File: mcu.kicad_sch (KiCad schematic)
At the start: 1 part

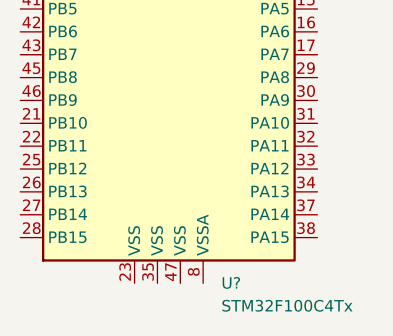
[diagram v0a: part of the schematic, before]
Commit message: wired up Nixie tubes
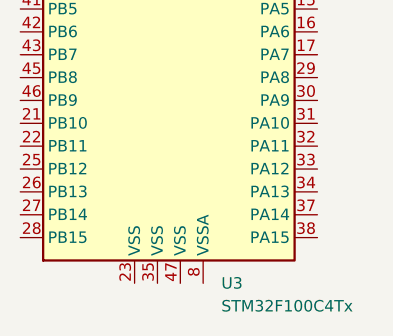
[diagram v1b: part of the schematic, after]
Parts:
- gave numbers to parts that had none: 1
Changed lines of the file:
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@@
   (symbol (lib_id "MCU_ST_STM32F1:STM32F100C4Tx") (at 148.59 86.36 0) (unit 1)
     (in_bom yes) (on_board yes) (fields_autoplaced)
-    (property "Reference" "U?" (id 0) (at 153.1494 124.46 0)
+    (property "Reference" "U3" (id 0) (at 153.1494 124.46 0)
       (effects (font (size 1.27 1.27)) (justify left))
     )

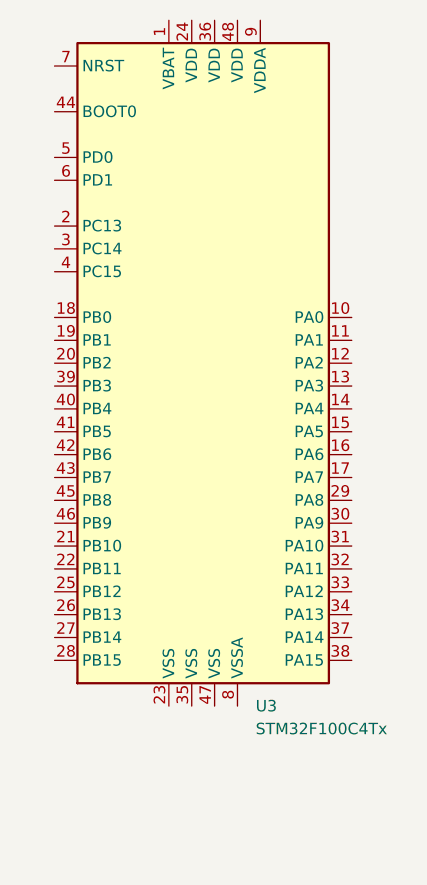
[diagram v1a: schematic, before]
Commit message: Added level shifter and finished up HV Shift Register page
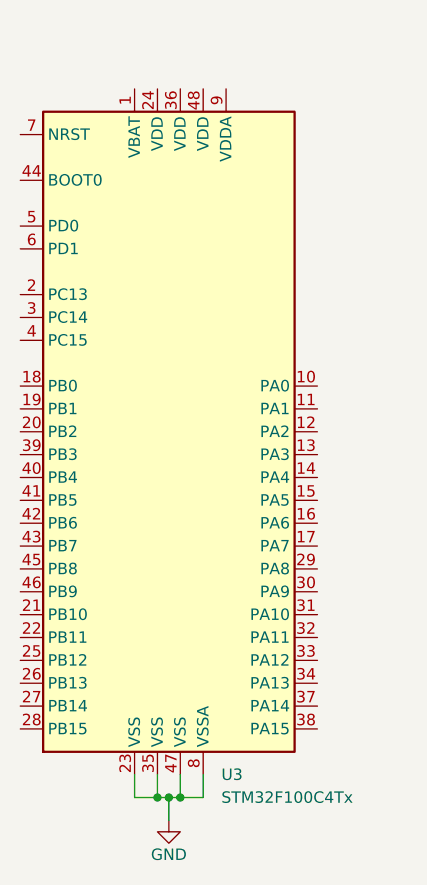
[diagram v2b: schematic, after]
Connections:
- net GND: now reaches U3.23 (VSS)
- net GND: now also U3.35 (VSS), U3.47 (VSS), U3.8 (VSSA)
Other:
- moved on the sheet: U3
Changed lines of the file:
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@@
 (kicad_sch (version 20211123) (generator eeschema)
   (paper "A4")
-  (symbol (lib_id "MCU_ST_STM32F1:STM32F100C4Tx") (at 148.59 86.36 0) (unit 1)
+  (junction (at 143.51 134.62) (diameter 0) (color 0 0 0 0)
+  )
+  (junction (at 144.78 134.62) (diameter 0) (color 0 0 0 0)
+  )
+  (junction (at 142.24 134.62) (diameter 0) (color 0 0 0 0)
+  )
+  (wire (pts (xy 142.24 132.08) (xy 142.24 134.62))
+    (stroke (width 0) (type default) (color 0 0 0 0))
+  )
+  (wire (pts (xy 147.32 132.08) (xy 147.32 134.62))
+    (stroke (width 0) (type default) (color 0 0 0 0))
+  )
+  (wire (pts (xy 144.78 134.62) (xy 143.51 134.62))
+    (stroke (width 0) (type default) (color 0 0 0 0))
+  )
+  (wire (pts (xy 147.32 134.62) (xy 144.78 134.62))
+    (stroke (width 0) (type default) (color 0 0 0 0))
+  )
+  (wire (pts (xy 139.7 132.08) (xy 139.7 134.62))
+    (stroke (width 0) (type default) (color 0 0 0 0))
+  )
+  (wire (pts (xy 142.24 134.62) (xy 139.7 134.62))
+    (stroke (width 0) (type default) (color 0 0 0 0))
+  )
+  (wire (pts (xy 143.51 134.62) (xy 143.51 137.16))
+    (stroke (width 0) (type default) (color 0 0 0 0))
+  )
+  (wire (pts (xy 143.51 134.62) (xy 142.24 134.62))
+    (stroke (width 0) (type default) (color 0 0 0 0))
+  )
+  (wire (pts (xy 144.78 132.08) (xy 144.78 134.62))
+    (stroke (width 0) (type default) (color 0 0 0 0))
+  )
+  (symbol (lib_id "MCU_ST_STM32F1:STM32F100C4Tx") (at 144.78 93.98 0) (unit 1)
     (in_bom yes) (on_board yes) (fields_autoplaced)
-    (property "Reference" "U3" (id 0) (at 153.1494 124.46 0)
+    (property "Reference" "U3" (id 0) (at 149.3394 132.08 0)
       (effects (font (size 1.27 1.27)) (justify left))
     )
-    (property "Value" "STM32F100C4Tx" (id 1) (at 153.1494 127 0)
+    (property "Value" "STM32F100C4Tx" (id 1) (at 149.3394 134.62 0)
       (effects (font (size 1.27 1.27)) (justify left))
     )
-    (property "Footprint" "Package_QFP:LQFP-48_7x7mm_P0.5mm" (id 2) (at 133.35 121.92 0)
+    (property "Footprint" "Package_QFP:LQFP-48_7x7mm_P0.5mm" (id 2) (at 129.54 129.54 0)
       (effects (font (size 1.27 1.27)) (justify right) hide)
     )
-    (property "Datasheet" "http://www.st.com/st-web-ui/static/active/en/resource/technical/document/datasheet/CD00251732.pdf" (id 3) (at 148.59 86.36 0)
+    (property "Datasheet" "http://www.st.com/st-web-ui/static/active/en/resource/technical/document/datasheet/CD00251732.pdf" (id 3) (at 144.78 93.98 0)
       (effects (font (size 1.27 1.27)) hide)
     )
@@
     (pin "9")
   )
+  (symbol (lib_id "power:GND") (at 143.51 137.16 0) (unit 1)
+    (in_bom yes) (on_board yes)
+    (property "Reference" "#PWR05" (id 0) (at 143.51 143.51 0)
+      (effects (font (size 1.27 1.27)) hide)
+    )
+    (property "Value" "GND" (id 1) (at 143.51 140.97 0))
+    (property "Footprint" "" (id 2) (at 143.51 137.16 0)
+      (effects (font (size 1.27 1.27)) hide)
+    )
+    (property "Datasheet" "" (id 3) (at 143.51 137.16 0)
+      (effects (font (size 1.27 1.27)) hide)
+    )
+    (pin "1")
+  )
 )
